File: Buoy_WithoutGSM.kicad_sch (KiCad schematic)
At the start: 9 parts, among them J1 Conn_01x02_Female, J2 Conn_01x05_Male, J6 Conn_VCC_ESP32, U1 Ultimate_GPS, U2 ESP32-DEVKITC-32D, U3 RFM95W_Board, U4 Ethernet-FeatherWing

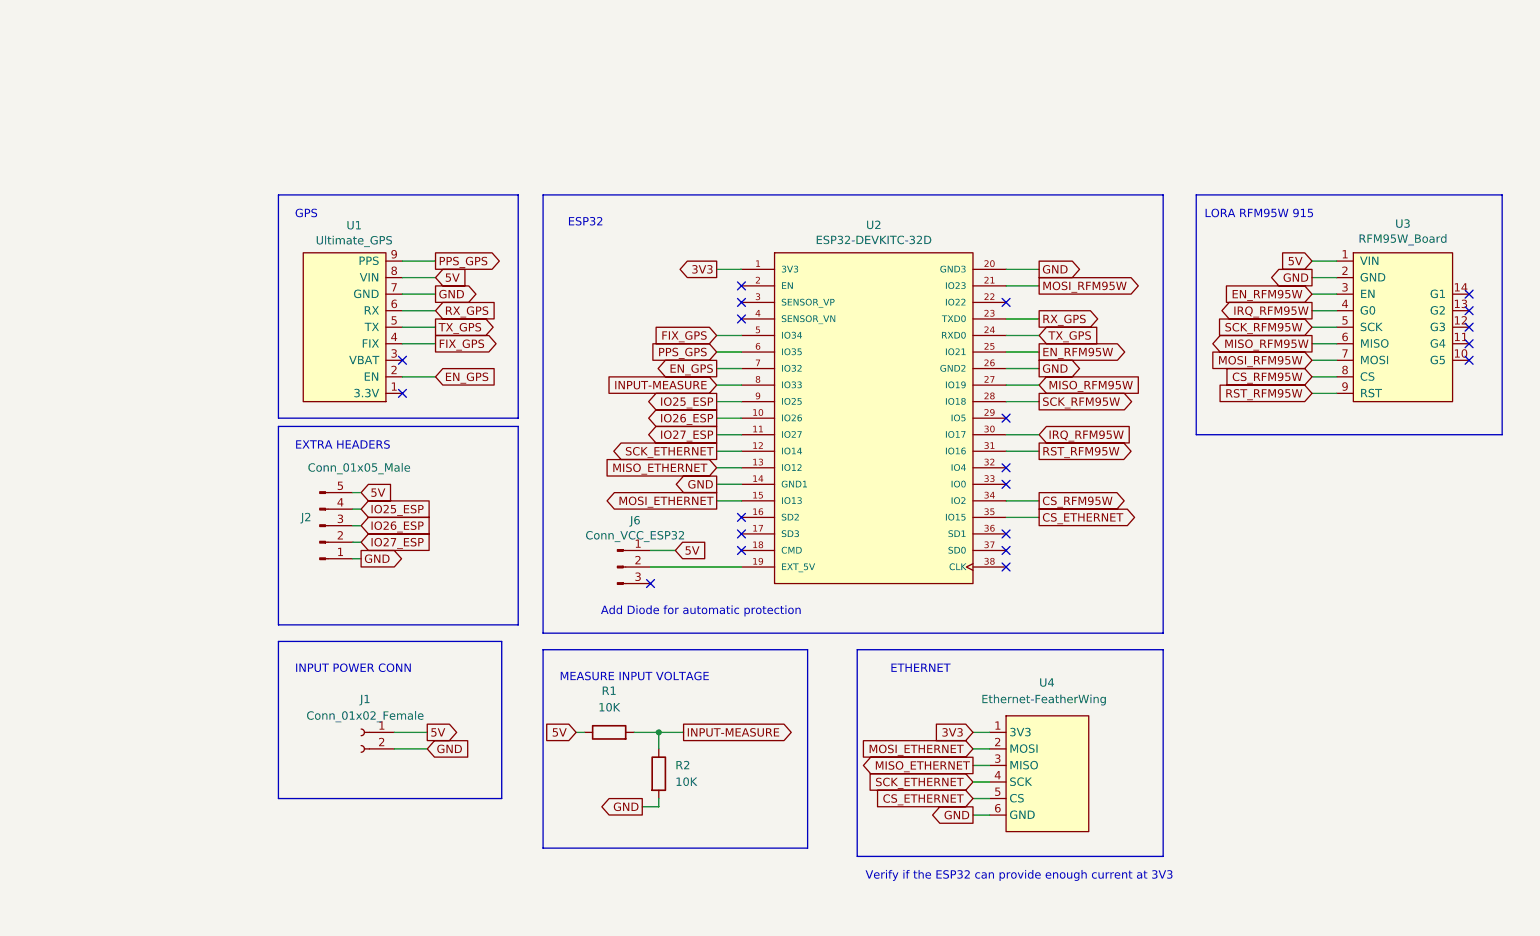
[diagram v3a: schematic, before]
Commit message: Changed toutes of the PCB, including routes width
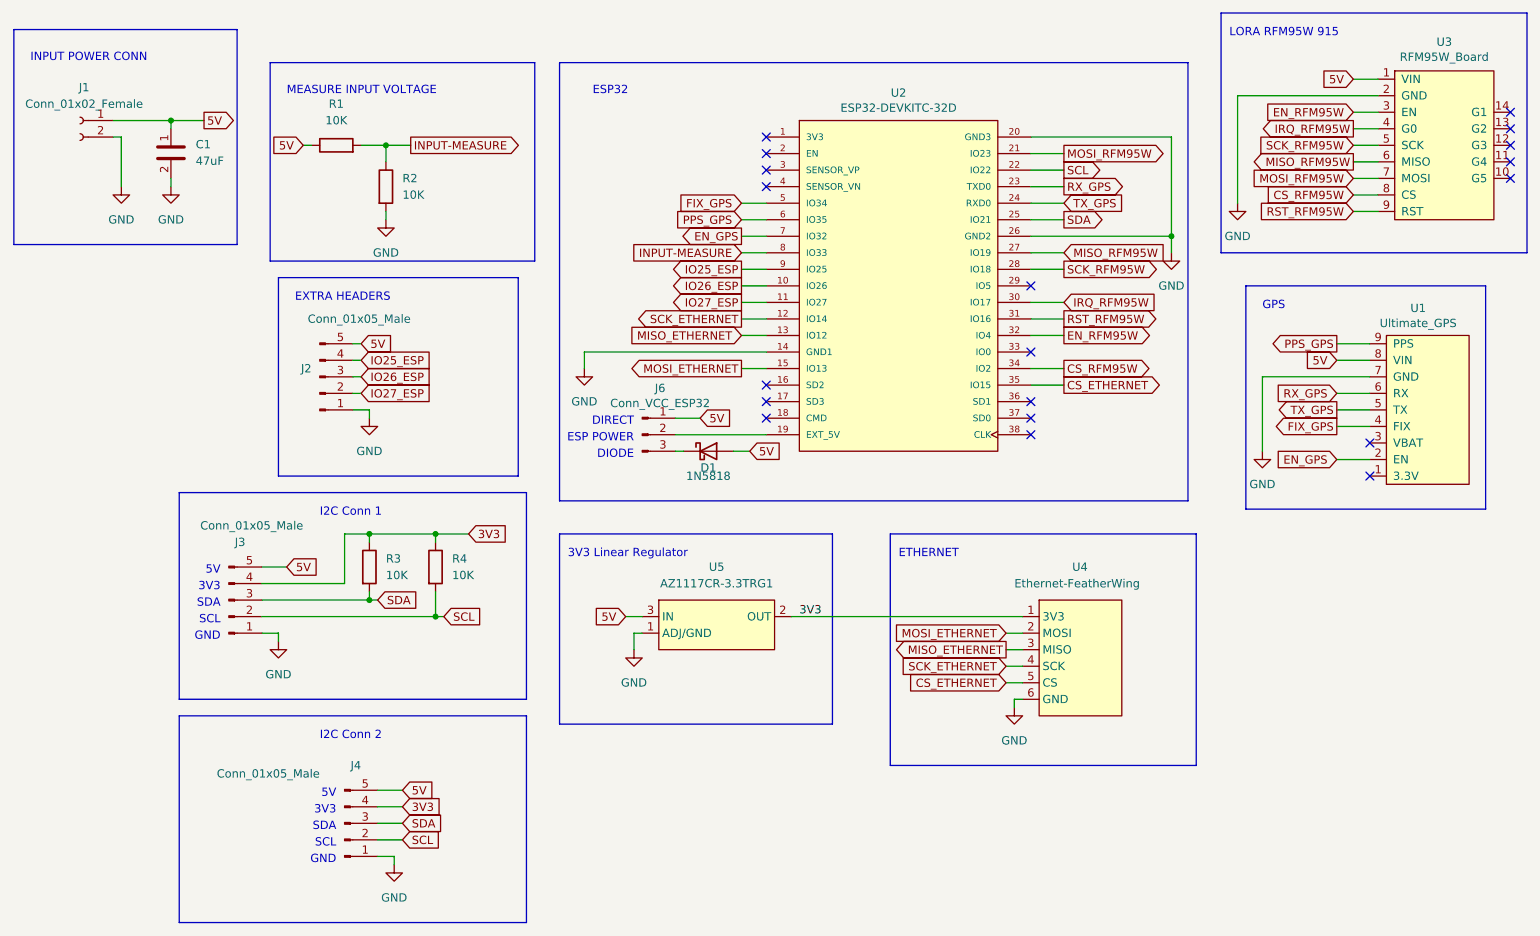
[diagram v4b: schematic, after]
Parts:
- added C1: 47uF, Resistor_SMD:R_0805_2012Metric_Pad1.20x1.40mm_HandSolder, symbol C-47uF-0805-10V:47uF
- added D1: 1N5818, Diode_THT:D_DO-41_SOD81_P10.16mm_Horizontal, symbol Diode:1N5818
- added J3, J4: Conn_01x05_Male, Connector_PinSocket_2.54mm:PinSocket_1x05_P2.54mm_Vertical, symbol Connector:Conn_01x05_Male
- added R3, R4: 10K, Resistor_SMD:R_0805_2012Metric, symbol R-10K-0805:10K
- added U5: AZ1117CR-3.3TRG1, Package_TO_SOT_SMD:SOT-89-3_Handsoldering, symbol AZ1117CR-3_3TRG1:AZ1117CR-3.3TRG1
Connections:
- net 3V3: now also J3.4 (Pin_4), J4.4 (Pin_4), R3.1, R4.1, U5.2 (OUT); no longer U2.1 (3V3)
- net 5V: now also C1.1, D1.2 (A), J3.5 (Pin_5), J4.5 (Pin_5), U5.3 (IN)
- net EN_RFM95W: now also U2.32 (IO4); no longer U2.25 (IO21)
- net GND: now also C1.2, J3.1 (Pin_1), J4.1 (Pin_1), U5.1 (ADJ/GND)
- net SCL: now reaches U2.22 (IO22)
- net SCL: now also J3.2 (Pin_2), J4.2 (Pin_2), R4.2
- net at J6.3 (Pin_3): now also D1.1 (K)
- new net SDA: J3.3 (Pin_3), J4.3 (Pin_3), R3.2, U2.25 (IO21)
- no-connect marks 21 -> 19
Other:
- note added: "3V3"
- note added: "3V3 Linear Regulator"
- note added: "5V"
- note added: "DIODE"
- note added: "DIRECT"
- note added: "ESP POWER"
- note added: "GND"
- note added: "I2C Conn 1"
- note added: "I2C Conn 2"
- note added: "SCL"
- note added: "SDA"
- note removed: "Add Diode for automatic protection"
- note removed: "Verify if the ESP32 can provide enough current at 3V3"
- moved on the sheet: J1, J2, J6, R1, R2, U1, U2, U3, U4
